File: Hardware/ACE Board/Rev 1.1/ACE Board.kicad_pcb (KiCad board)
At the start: 2 copper layers, 335 x 250 mm, 204 parts, among them J1 PHI2 SELECT, J10 PORT A, J11 AUDIO L, J12 DB9 MALE (DTE), J13 PS/2, J14 KEYBOARD, J15 AUDIO R, J16 AUDIO, J17 5V DC, J18 CART, J19 BUS, J2 CTS EN, J20 VCC, J21 POWER LED, J22 STORAGE, J3 RESET SW, J4 DCD EN, J5 VDD, J6 JOYSTICK A, J7 PADDLES, J8 JOYSTICK B, J9 PORT B, SW1 `, SW10 9, SW11 0, SW12 -, SW13 =, SW14 BACKSPACE, SW15 ESCAPE, SW16 TAB, SW17 RESET, SW18 Q, SW19 W, SW2 1, SW20 E, SW21 R, SW22 T, SW23 Y, SW24 U, SW25 I, SW26 O, SW27 P, SW28 [, SW29 ], SW3 2, SW30 \, SW31 INSERT, SW32 CAPS LOCK, SW33 A, SW34 S, SW35 D, SW36 F, SW37 G, SW38 H, SW39 J, SW4 3, SW40 K, SW41 L, SW42 SHIFT, SW43 ;, SW44 ', SW45 ENTER, SW46 DELETE, SW47 Z, SW48 X, SW49 C, SW5 4, SW50 SHIFT, SW51 V, SW52 B, SW53 N, SW54 M, SW55 ,, SW56 ., SW57 /, SW58 UP ARROW, SW59 CTRL, SW6 5, SW60 ALT, SW61 MENU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

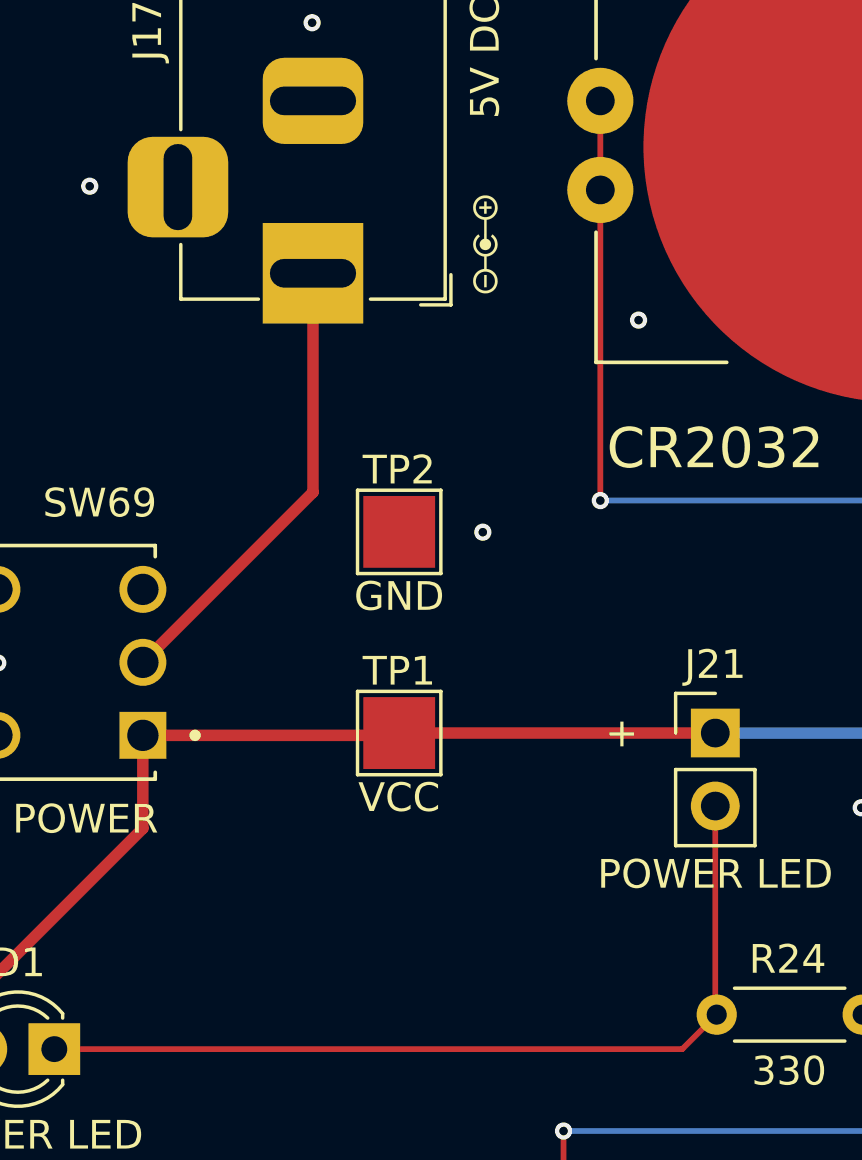
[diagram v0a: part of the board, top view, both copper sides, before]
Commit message: Add bulk capacitance to Rev 1.1
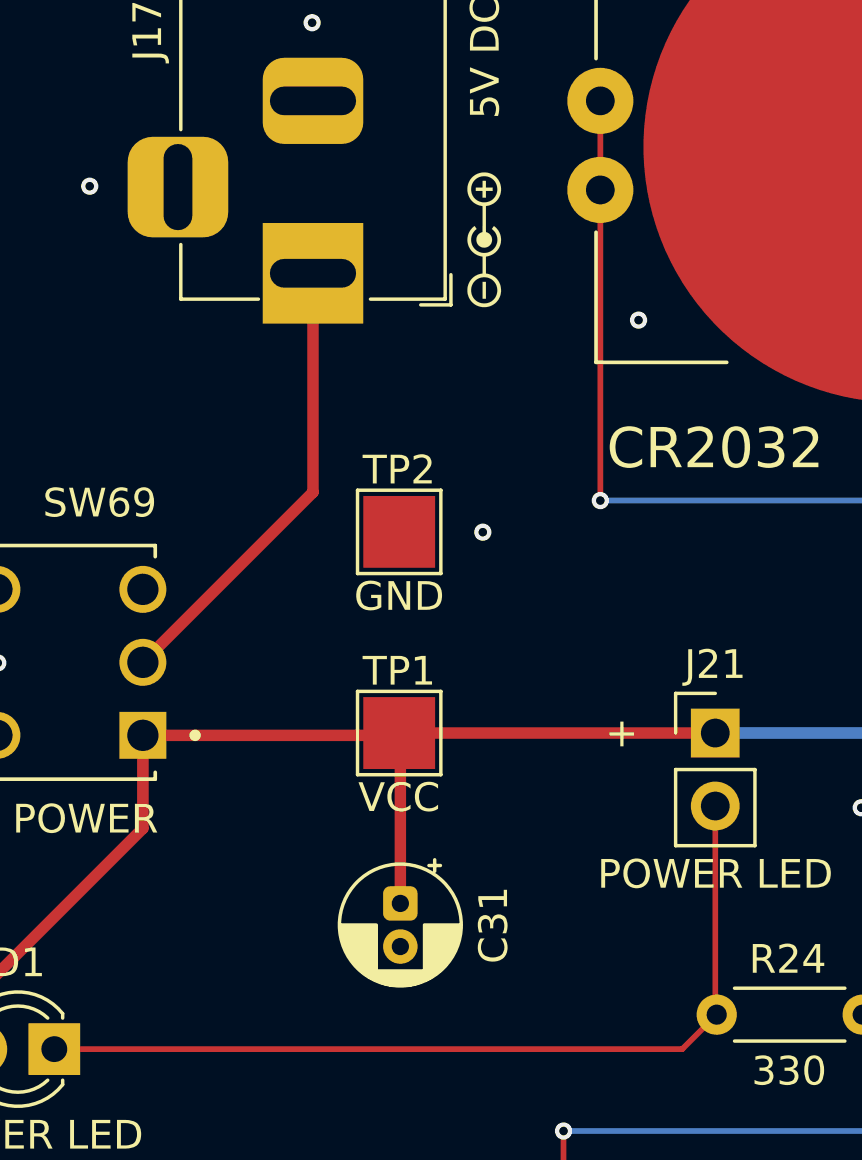
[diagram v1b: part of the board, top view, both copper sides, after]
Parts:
- added C31: 10uF, Capacitor_THT:CP_Radial_D4.0mm_P1.50mm, F.Cu at (123.0, 110.9)
- moved REF** 0.16 mm to (126.0, 87.8)
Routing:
- net VCC: track 1445.4 -> 1451.3 mm
